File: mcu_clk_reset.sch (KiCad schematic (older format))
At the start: 18 parts

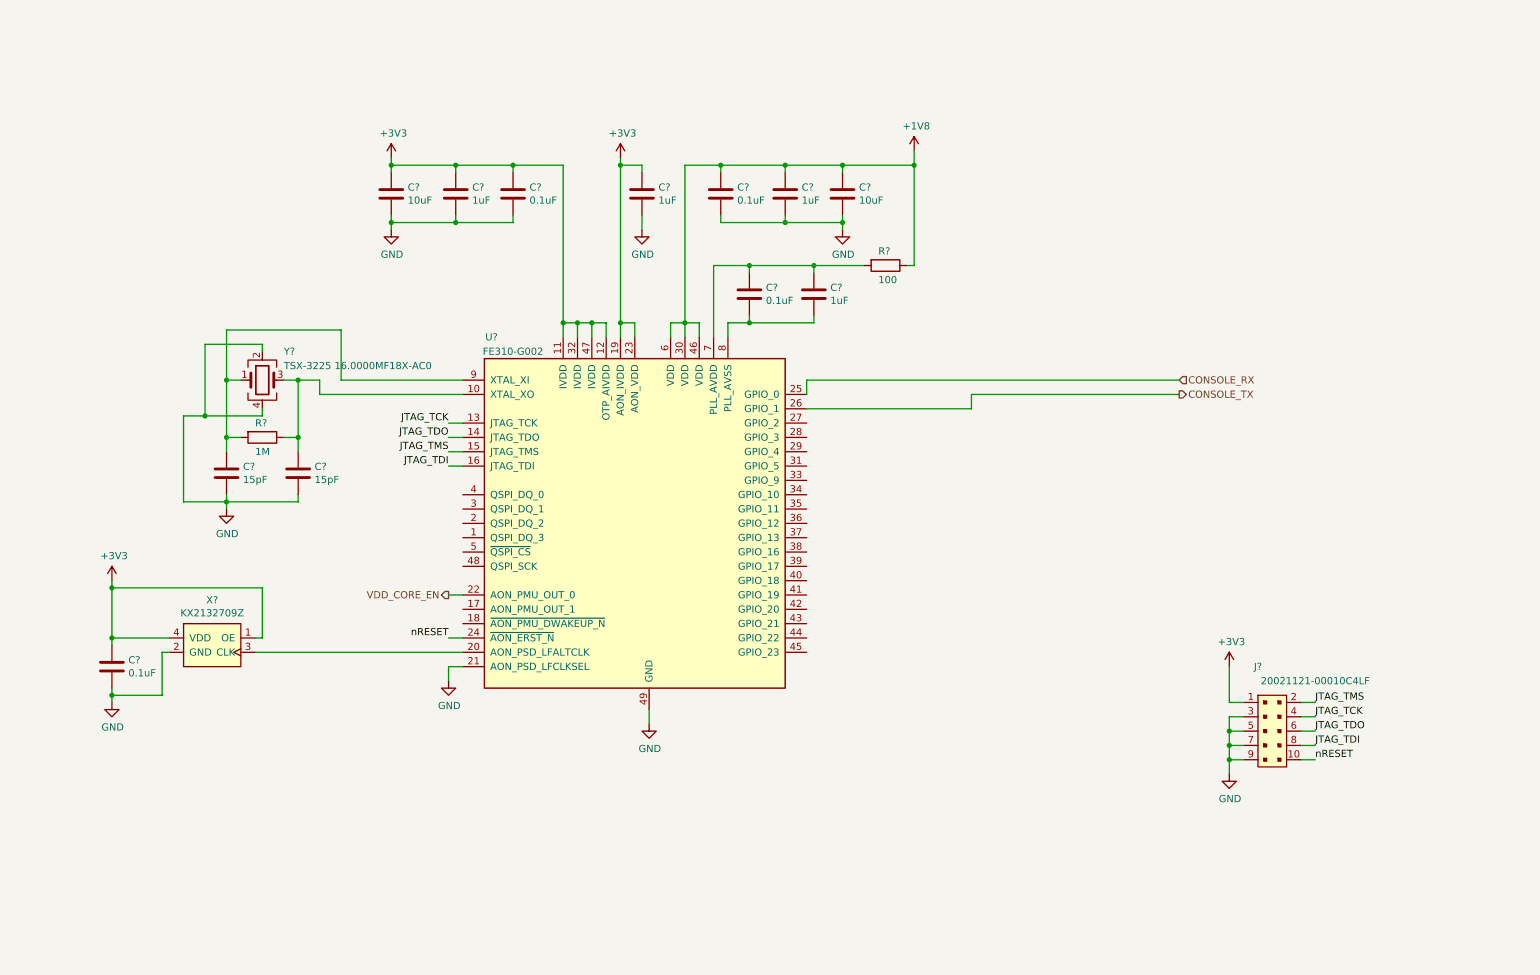
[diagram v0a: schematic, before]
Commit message: Update LEDs descriptions, add main osc footprint
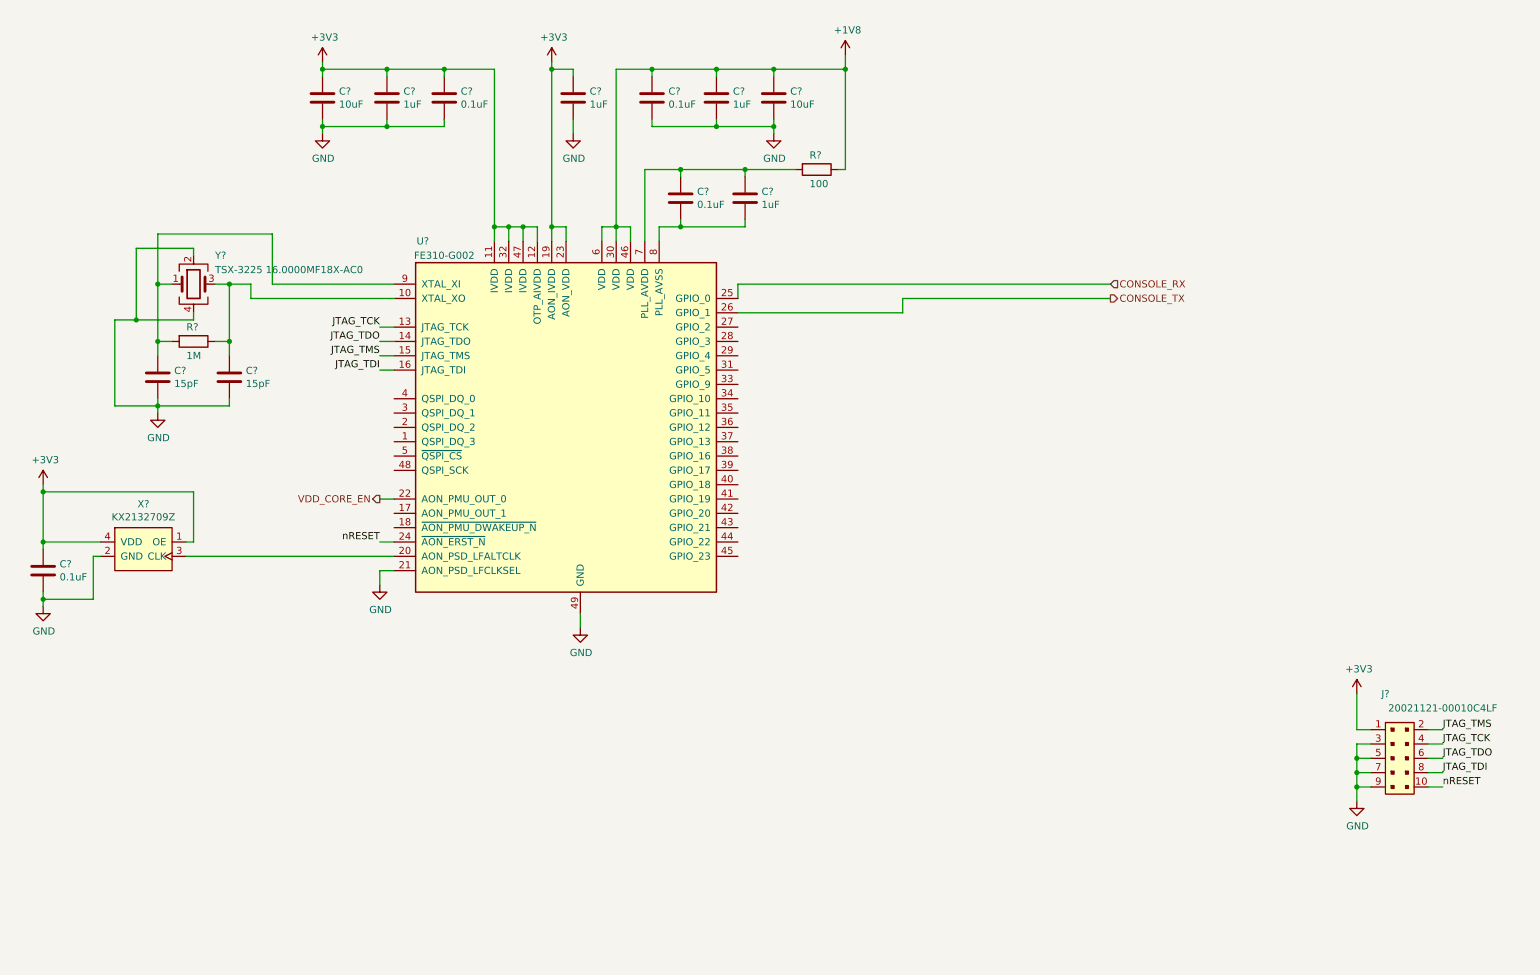
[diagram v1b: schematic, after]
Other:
- moved on the sheet: C?, J?, R?, U?, X?, Y?

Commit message: Change main MCU footprint
Now it has a big hole in the back which will help me connecting it to GND
with a soldering iron.
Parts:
- removed U?: FE310-G002, Package_DFN_QFN:QFN-48-1EP_6x6mm_P0.4mm_EP4.2x4.2mm_ThermalVias, symbol himudev:FE310-G002
- added U?: FE310-G002, himudev:QFN-48-1EP_6x6mm_P0.4mm_EP4.2x4.2mm_BigVia, symbol himudev:FE310-G002
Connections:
- net +1V8: now also U?.30 (VDD), U?.46 (VDD), U?.6 (VDD)
- net +3V3: now also U?.11 (IVDD), U?.12 (OTP_AIVDD), U?.19 (AON_IVDD), U?.23 (AON_VDD), U?.32 (IVDD), U?.47 (IVDD)
- net CONSOLE_RX: now also U?.38 (GPIO_16)
- net CONSOLE_TX: now also U?.39 (GPIO_17)
- net GND: now also U?.21 (AON_PSD_LFCLKSEL), U?.49 (GND)
- net JTAG_TCK: now also U?.13 (JTAG_TCK)
- net JTAG_TDI: now also U?.16 (JTAG_TDI)
- net JTAG_TDO: now also U?.14 (JTAG_TDO)
- net JTAG_TMS: now also U?.15 (JTAG_TMS)
- net VDD_CORE_EN: now also U?.22 (AON_PMU_OUT_0)
- net nRESET: now also U?.24 (~AON_ERST_N)
- net at X?.3 (CLK): now also U?.20 (AON_PSD_LFALTCLK)
- net at C?.1, R?.1, Y?.3: now also U?.10 (XTAL_XO)
- net at C?.1, C?.1, R?.2: now also U?.7 (PLL_AVDD)
- net at C?.2, C?.2: now also U?.8 (PLL_AVSS)
- net at C?.1, R?.2, Y?.1: now also U?.9 (XTAL_XI)
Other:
- moved on the sheet: C?, J?, R?, X?, Y?

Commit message: Select footprint for main osc
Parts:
- Y?: footprint (none) -> himudev:TSX-3225
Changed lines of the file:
@@
 F 0 "Y?" H 1950 2600 50  0000 L CNN
 F 1 "TSX-3225 16.0000MF18X-AC0" H 1950 2500 50  0000 L CNN
-F 2 "" H 1800 2400 50  0001 C CNN
+F 2 "himudev:TSX-3225" H 1800 2400 50  0001 C CNN
 F 3 "~" H 1800 2400 50  0001 C CNN
 	1    1800 2400

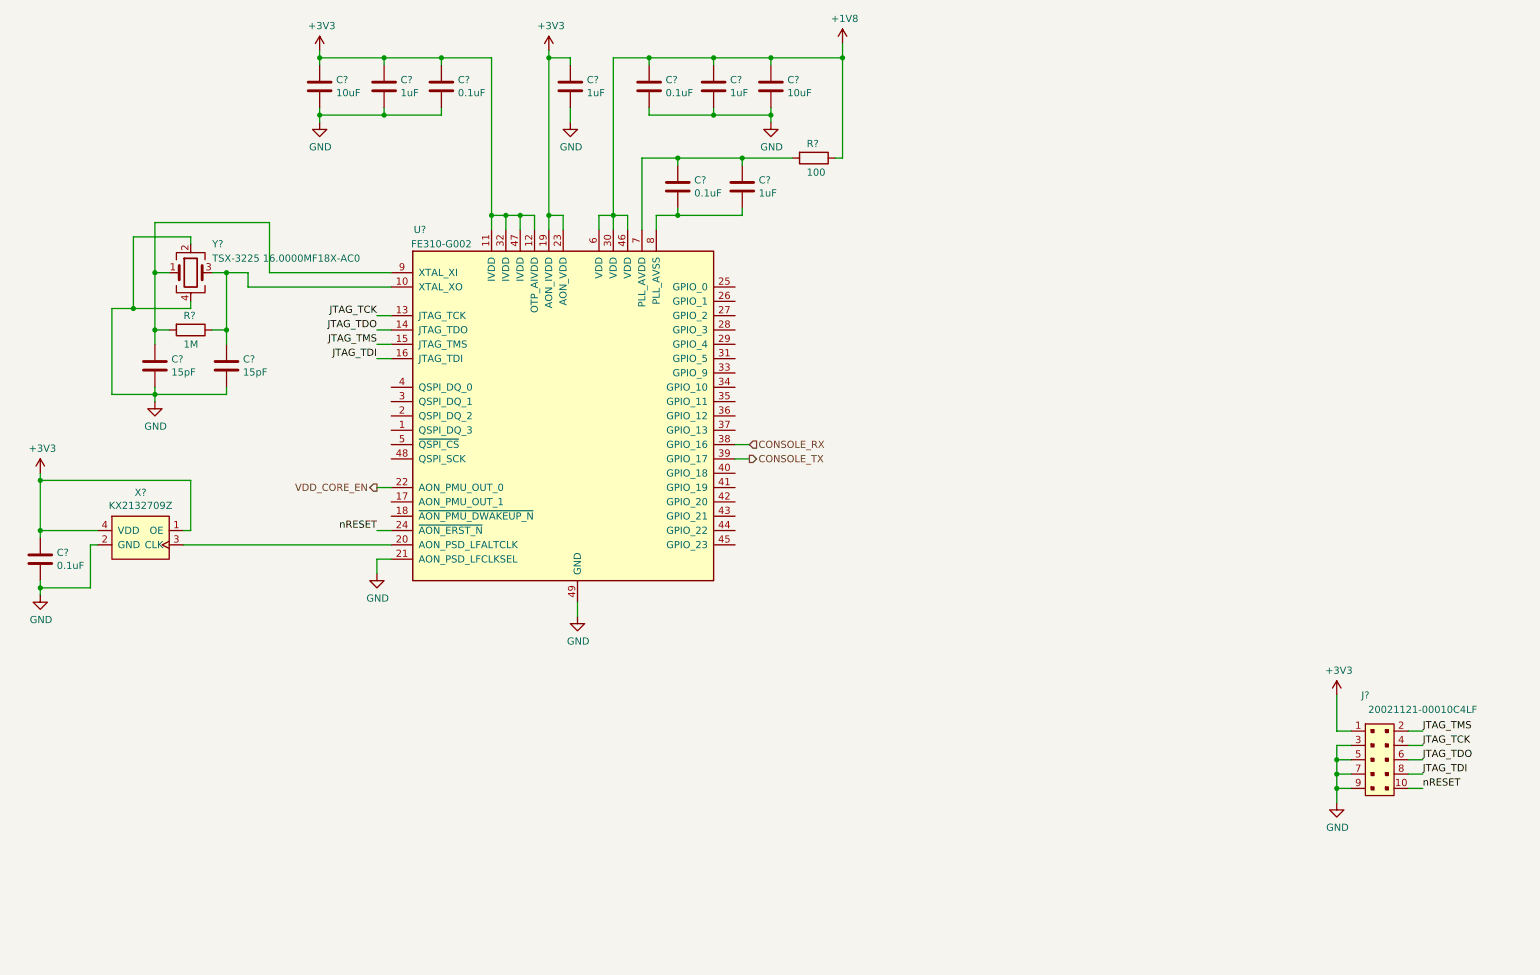
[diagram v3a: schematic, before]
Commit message: Add QSPI flash
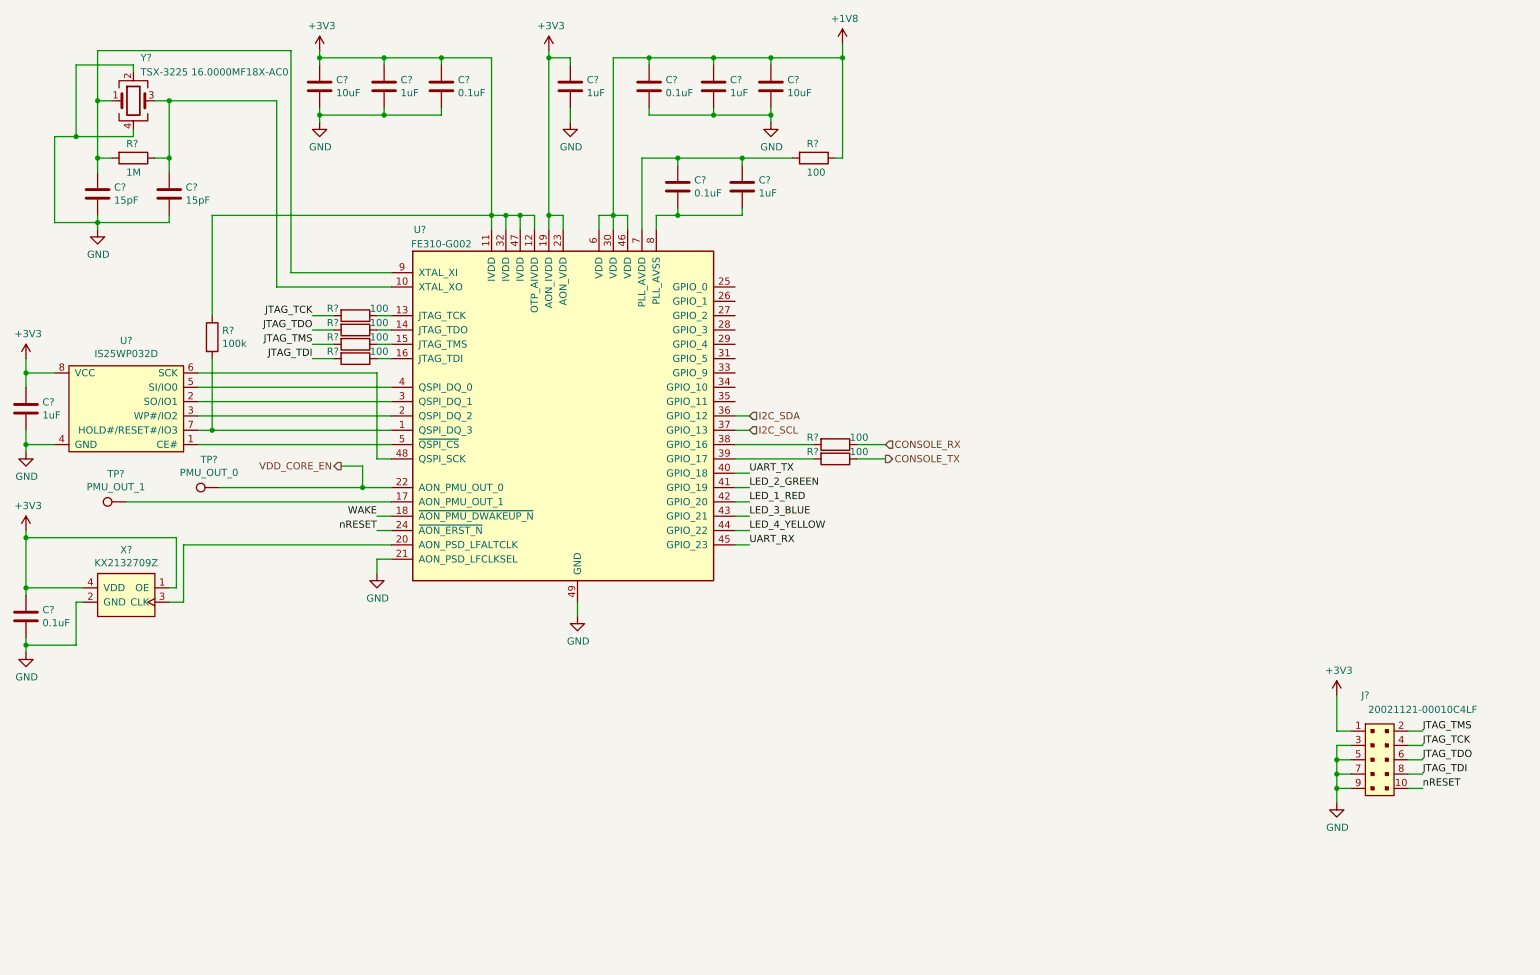
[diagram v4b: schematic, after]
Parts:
- added C?: 1uF, symbol Device:C
- added R? (x6): 100, symbol Device:R
- added R?: 100k, symbol Device:R
- added TP?: PMU_OUT_1, symbol Connector:TestPoint
- added TP?: PMU_OUT_0, symbol Connector:TestPoint
- added U?: IS25WP032D, Package_SO:SOIC-8_3.9x4.9mm_P1.27mm, symbol himudev:IS25WP032D
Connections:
- net +3V3: now also C?.1, R?.1, U?.8 (VCC)
- net CONSOLE_RX: now also R?.1; no longer U?.38 (GPIO_16)
- net CONSOLE_TX: now also R?.1; no longer U?.39 (GPIO_17)
- net GND: now also C?.2, U?.4 (GND)
- net JTAG_TCK: now also R?.2; no longer U?.13 (JTAG_TCK)
- net JTAG_TDI: now also R?.2; no longer U?.16 (JTAG_TDI)
- net JTAG_TDO: now also R?.2; no longer U?.14 (JTAG_TDO)
- net JTAG_TMS: now also R?.2; no longer U?.15 (JTAG_TMS)
- net VDD_CORE_EN: now also TP?.1
- net at U?.1 (QSPI_DQ_3): now also R?.2, U?.7 (HOLD#/RESET#/IO3)
- net at U?.17 (AON_PMU_OUT_1): now also TP?.1
- net WAKE: now reaches U?.18 (~AON_PMU_DWAKEUP_N)
- net at U?.2 (QSPI_DQ_2): now also U?.3 (WP#/IO2)
- net at U?.3 (QSPI_DQ_1): now also U?.2 (SO/IO1)
- net I2C_SDA: now reaches U?.36 (GPIO_12)
- net I2C_SCL: now reaches U?.37 (GPIO_13)
- net at U?.4 (QSPI_DQ_0): now also U?.5 (SI/IO0)
- net UART_TX: now reaches U?.40 (GPIO_18)
- net LED_2_GREEN: now reaches U?.41 (GPIO_19)
- net LED_1_RED: now reaches U?.42 (GPIO_20)
- net LED_3_BLUE: now reaches U?.43 (GPIO_21)
- net LED_4_YELLOW: now reaches U?.44 (GPIO_22)
- net UART_RX: now reaches U?.45 (GPIO_23)
- net at U?.48 (QSPI_SCK): now also U?.6 (SCK)
- net at U?.5 (~QSPI_CS): now also U?.1 (CE#)
- new net: R?.1, U?.13 (JTAG_TCK)
- new net: R?.1, U?.14 (JTAG_TDO)
- new net: R?.1, U?.15 (JTAG_TMS)
- new net: R?.1, U?.16 (JTAG_TDI)
- new net: R?.2, U?.38 (GPIO_16)
- new net: R?.2, U?.39 (GPIO_17)
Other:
- moved on the sheet: C?, R?, X?, Y?

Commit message: First full version of a schematic
This commit is a quicksave of completed but not reviewed schematic.
Added pressure sensor, finished IMU wiring, finished top-level
schematic, added pin header, placed LEDs and many others.
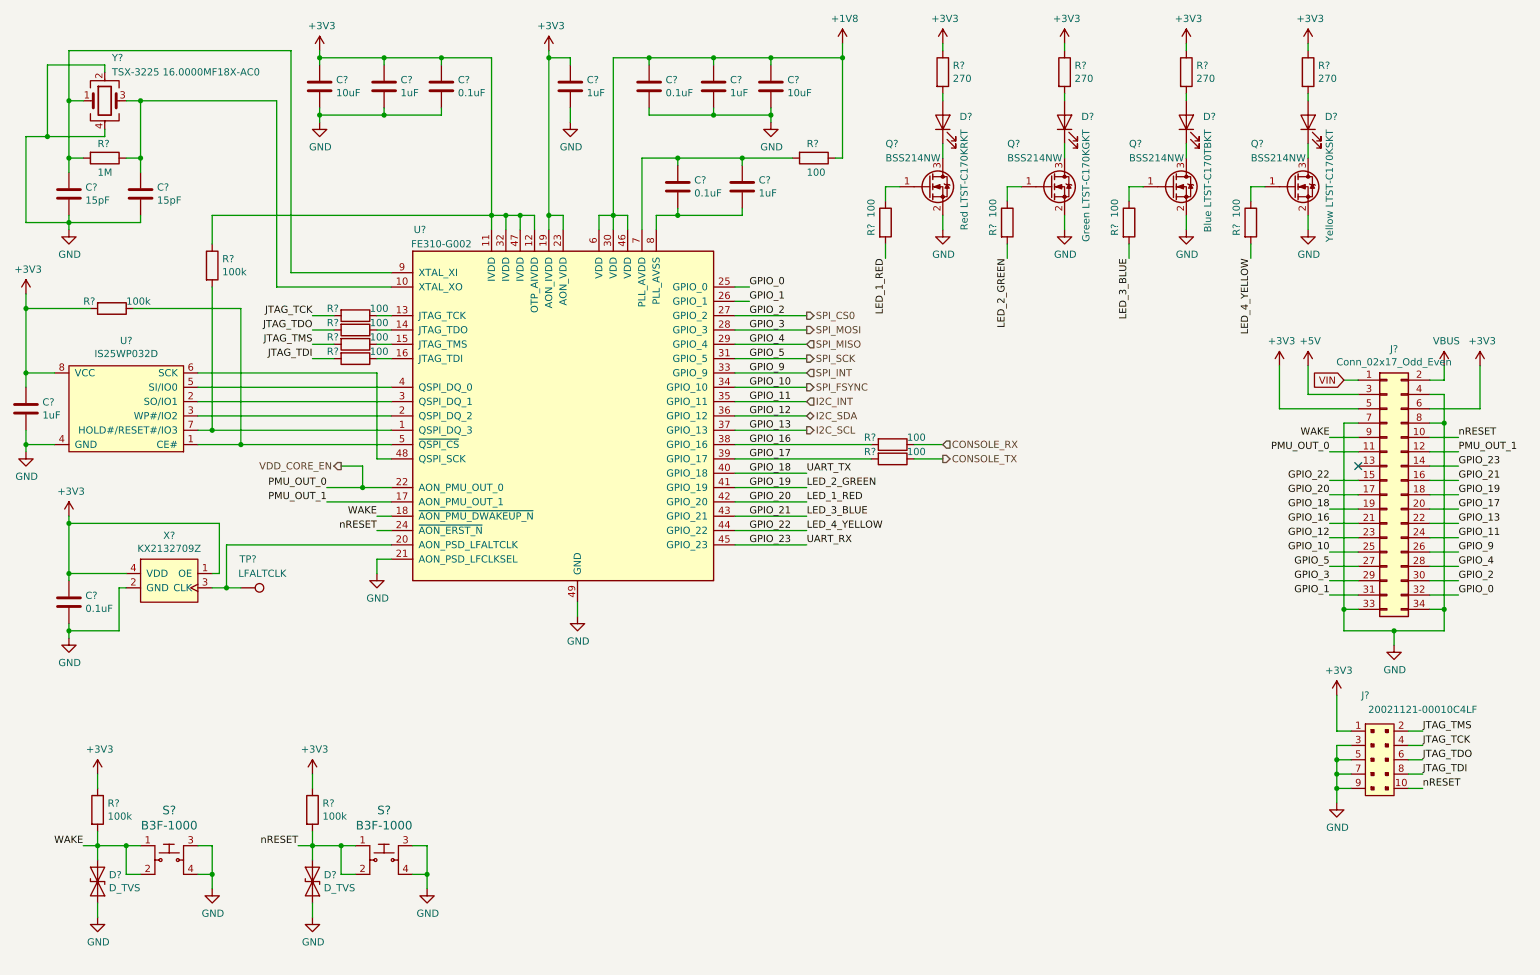
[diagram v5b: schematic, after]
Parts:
- removed TP?: PMU_OUT_1, symbol Connector:TestPoint
- removed TP?: PMU_OUT_0, symbol Connector:TestPoint
- added D? (x2): D_TVS, symbol Device:D_TVS
- added D?: Green LTST-C170KGKT, symbol Device:LED
- added D?: Red LTST-C170KRKT, symbol Device:LED
- added D?: Yellow LTST-C170KSKT, symbol Device:LED
- added D?: Blue LTST-C170TBKT, symbol Device:LED
- added J?: Conn_02x17_Odd_Even, symbol Connector_Generic:Conn_02x17_Odd_Even
- added Q? (x4): BSS214NW, Package_TO_SOT_SMD:SOT-323_SC-70, symbol Transistor_FET:BSS214NW
- added R? (x3): 100k, symbol Device:R
- added R? (x4): 270, symbol Device:R
- added R? (x4): 100, symbol Device:R
- added S? (x2): B3F-1000, digikey-footprints:Switch_Tactile_THT_B3F-1xxx, symbol dk_Tactile-Switches:B3F-1000
- added TP?: LFALTCLK, symbol Connector:TestPoint
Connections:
- net +3V3: now also J?.5 (Pin_5), J?.6 (Pin_6), R?.1, R?.1, R?.1, R?.1, R?.1, R?.1, R?.2
- net GND: now also D?.2 (A2), D?.2 (A2), J?.33 (Pin_33), J?.34 (Pin_34), J?.4 (Pin_4), J?.7 (Pin_7), J?.8 (Pin_8), Q?.2 (S), Q?.2 (S), Q?.2 (S), Q?.2 (S), S?.3, S?.3, S?.4, S?.4
- net I2C_SCL: now also J?.22 (Pin_22)
- net I2C_SDA: now also J?.23 (Pin_23)
- net VDD_CORE_EN: now also J?.11 (Pin_11)
- net WAKE: now also D?.1 (A1), J?.9 (Pin_9), R?.2, S?.1, S?.2
- net nRESET: now also D?.1 (A1), J?.10 (Pin_10), R?.2, S?.1, S?.2
- net at U?.20 (AON_PSD_LFALTCLK), X?.3 (CLK): now also TP?.1
- net PMU_OUT_1: now reaches U?.17 (AON_PMU_OUT_1)
- net PMU_OUT_1: now also J?.12 (Pin_12)
- net GPIO_0: now reaches U?.25 (GPIO_0)
- net GPIO_0: now also J?.32 (Pin_32)
- net GPIO_1: now reaches U?.26 (GPIO_1)
- net GPIO_1: now also J?.31 (Pin_31)
- net SPI_CS0: now reaches U?.27 (GPIO_2)
- net SPI_CS0: now also J?.30 (Pin_30)
- net SPI_MOSI: now reaches U?.28 (GPIO_3)
- net SPI_MOSI: now also J?.29 (Pin_29)
- net SPI_MISO: now reaches U?.29 (GPIO_4)
- net SPI_MISO: now also J?.28 (Pin_28)
- net SPI_SCK: now reaches U?.31 (GPIO_5)
- net SPI_SCK: now also J?.27 (Pin_27)
- net SPI_INT: now reaches U?.33 (GPIO_9)
- net SPI_INT: now also J?.26 (Pin_26)
- net SPI_FSYNC: now reaches U?.34 (GPIO_10)
- net SPI_FSYNC: now also J?.25 (Pin_25)
- net I2C_INT: now reaches U?.35 (GPIO_11)
- net I2C_INT: now also J?.24 (Pin_24)
- net GPIO_16: now reaches R?.2, U?.38 (GPIO_16)
- net GPIO_16: now also J?.21 (Pin_21)
- net GPIO_17: now reaches R?.2, U?.39 (GPIO_17)
- net GPIO_17: now also J?.20 (Pin_20)
- net at U?.1 (CE#), U?.5 (~QSPI_CS): now also R?.1
- net LED_1_RED renamed GPIO_20
- net GPIO_20: now also J?.17 (Pin_17), R?.2
- net LED_2_GREEN renamed GPIO_19
- net GPIO_19: now also J?.18 (Pin_18), R?.2
- net LED_3_BLUE renamed GPIO_21
- net GPIO_21: now also J?.16 (Pin_16), R?.2
- net LED_4_YELLOW renamed GPIO_22
- net GPIO_22: now also J?.15 (Pin_15), R?.2
- net UART_RX renamed GPIO_23
- net GPIO_23: now also J?.14 (Pin_14)
- net UART_TX renamed GPIO_18
- net GPIO_18: now also J?.19 (Pin_19)
- new net: Q?.1 (G), R?.1 (x4)
- new net: D?.1 (K), Q?.3 (D) (x4)
- new net: D?.2 (A), R?.2 (x4)
- new net +5V: J?.3 (Pin_3)
- new net VBUS: J?.2 (Pin_2)
- new net VIN: J?.1 (Pin_1)
- no-connect marks 0 -> 1
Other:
- moved on the sheet: C?, R?, X?, Y?
